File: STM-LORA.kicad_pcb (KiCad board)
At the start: 2 copper layers, 2 parts, among them U1 stm32f103c8t6-module-china, U2 RFM95HW

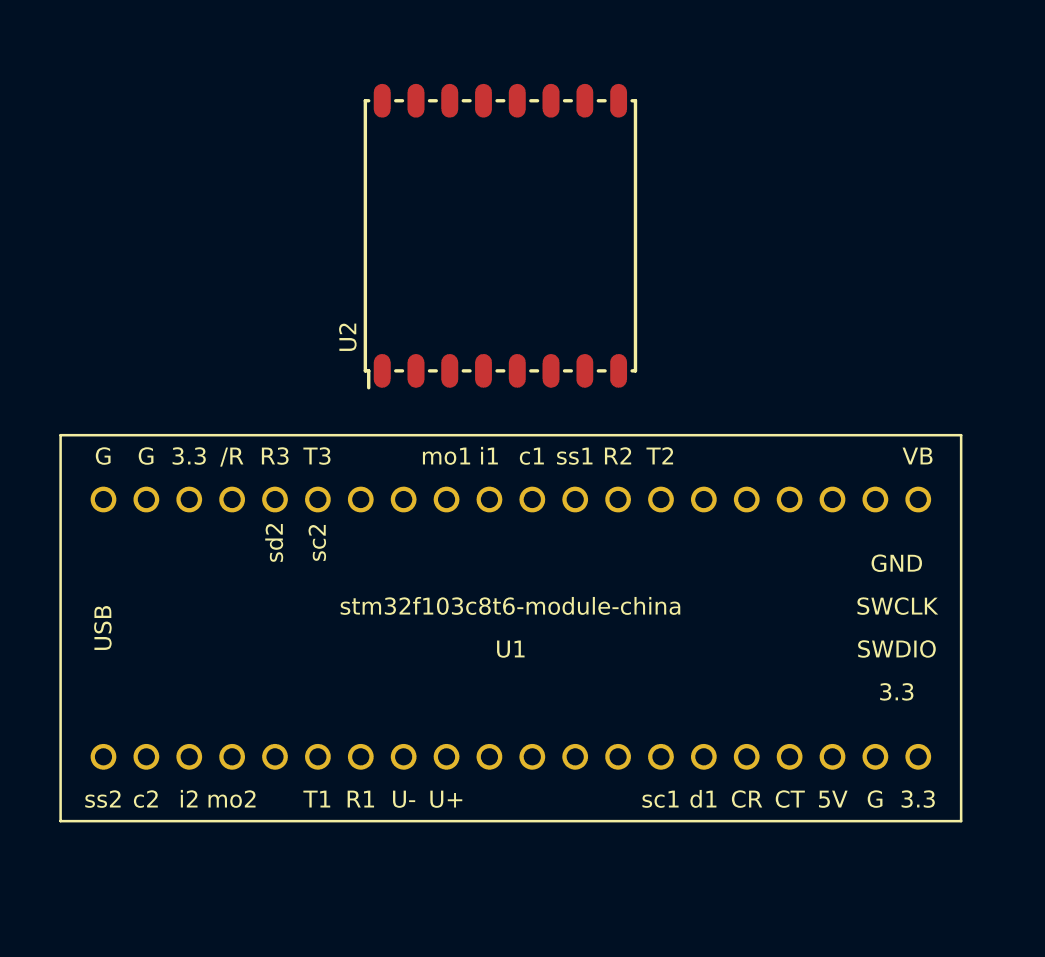
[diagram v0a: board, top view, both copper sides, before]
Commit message: Added power components
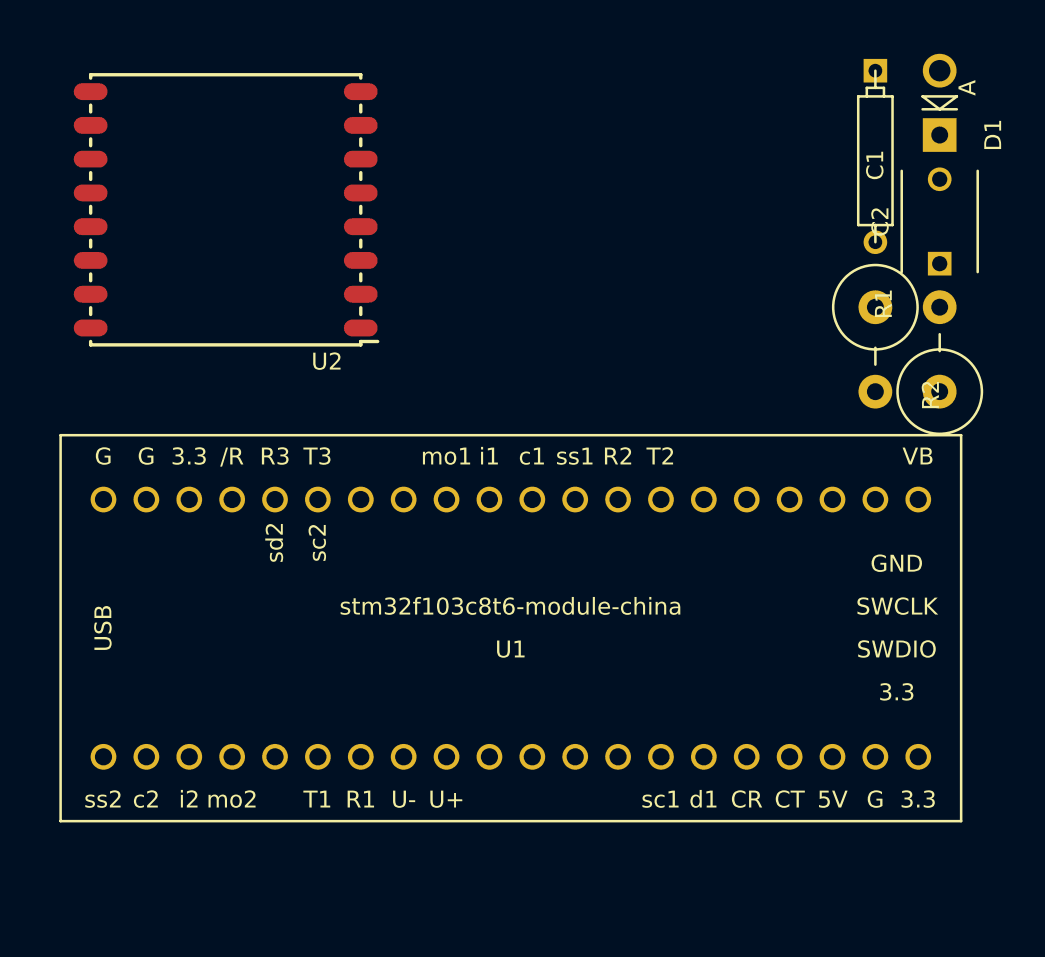
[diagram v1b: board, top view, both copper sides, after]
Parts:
- added C1: 100µ, Discret:CP4, F.Cu at (133.3, 62.2)
- added C2: 100n, Capacitors_ThroughHole:C_Disc_D6_P5, F.Cu at (137.2, 68.6)
- added D1: D_Schottky BAT85, Diodes_ThroughHole:Diode_DO-41_SOD81_Vertical_AnodeUp, F.Cu at (137.2, 61.0)
- added R1: 100k, Resistors_ThroughHole:Resistor_Vertical_RM5mm, F.Cu at (137.2, 73.7)
- added R2: 100k, Resistors_ThroughHole:Resistor_Vertical_RM5mm, F.Cu at (133.3, 73.7)
- moved U2 2.84 mm to (102.9, 72.4), turned to 180 degrees
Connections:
- net /3V3 renamed +3V3
- U1 pad 18: Net-(U1-Pad18) -> +BATT
- U1 pad 26: Net-(U1-Pad26) -> /BattTest

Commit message: update STM32 lib, add connectors
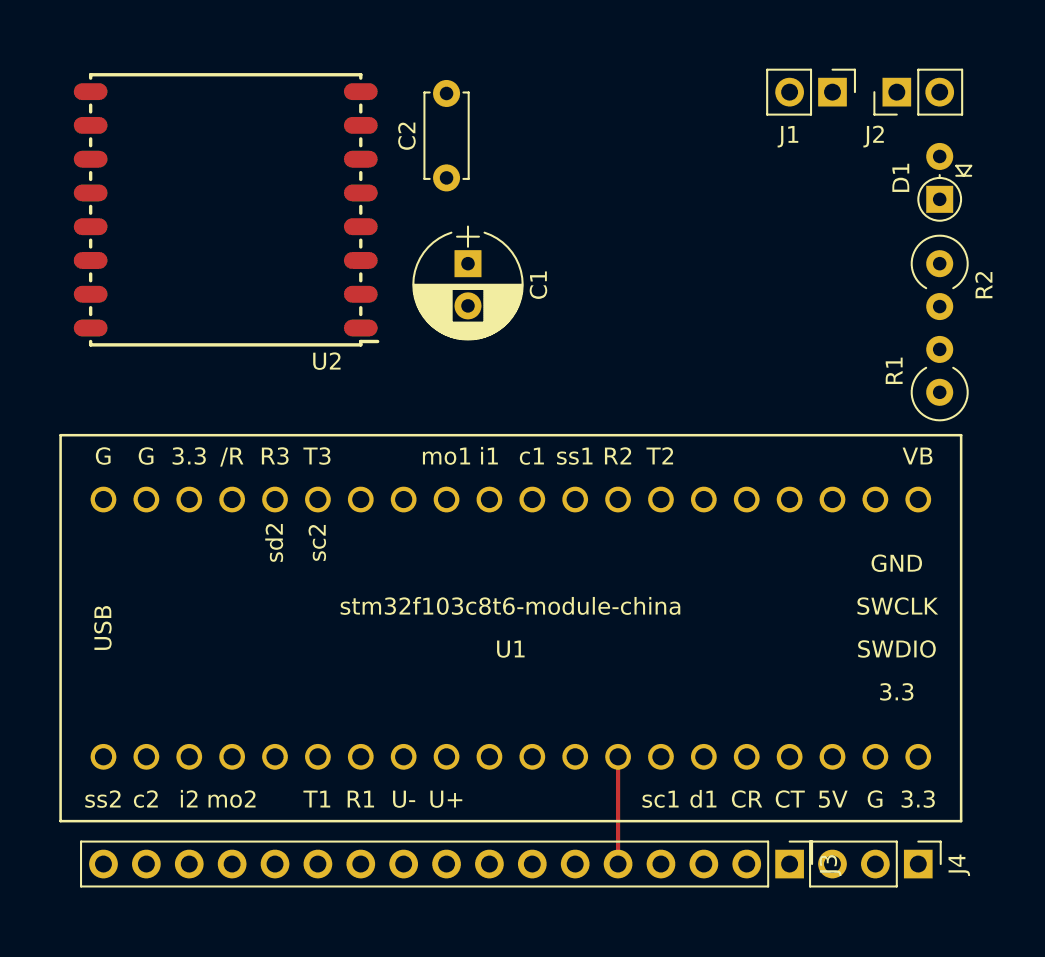
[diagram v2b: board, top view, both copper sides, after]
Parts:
- added J1: Batt, Pin_Headers:Pin_Header_Straight_1x02_Pitch2.54mm, F.Cu at (130.8, 58.4)
- added J2: Solar, Pin_Headers:Pin_Header_Straight_1x02_Pitch2.54mm, F.Cu at (134.6, 58.4)
- added J3: CONN_01X17, Socket_Strips:Socket_Strip_Straight_1x17_Pitch2.54mm, F.Cu at (128.3, 104.1)
- added J4: CONN_01X03, Pin_Headers:Pin_Header_Straight_1x03_Pitch2.54mm, F.Cu at (135.9, 104.1)
- C1: footprint Discret:CP4 -> Capacitors_THT:CP_Radial_D6.3mm_P2.50mm
- C2: footprint Capacitors_ThroughHole:C_Disc_D6_P5 -> Capacitors_THT:C_Disc_D5.0mm_W2.5mm_P5.00mm
- D1: value D_Schottky BAT85 -> BAT85; footprint Diodes_ThroughHole:Diode_DO-41_SOD81_Vertical_AnodeUp -> Diodes_THT:D_DO-35_SOD27_P2.54mm_Vertical_AnodeUp
- R1, R2: footprint Resistors_ThroughHole:Resistor_Vertical_RM5mm -> Resistors_THT:R_Axial_DIN0309_L9.0mm_D3.2mm_P2.54mm_Vertical
- moved C2 29.6 mm to (108.0, 63.5)
- moved C1 25.0 mm to (109.2, 68.6)
- moved R2 6.35 mm to (137.2, 68.6)
- moved D1 3.81 mm to (137.2, 64.8)
- moved R1 2.54 mm to (137.2, 76.2)
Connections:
- net +BATT renamed VCC
- D1 pad 2: +5V -> Net-(D1-Pad2)
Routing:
- net Net-(J3-Pad5): track 0.00 -> 6.35 mm

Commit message: start traces
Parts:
- added J5: CONN_01X03, Pin_Headers:Pin_Header_Straight_1x03_Pitch2.54mm, F.Cu at (87.6, 76.2)
- added J6: CONN_01X01, Pin_Headers:Pin_Header_Straight_1x01_Pitch2.54mm, F.Cu at (132.1, 76.2)
- added J7: CONN_01X14, Socket_Strips:Socket_Strip_Straight_1x14_Pitch2.54mm, F.Cu at (95.2, 76.2)
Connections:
- net +3V3 renamed /3V3
- net /BattTest renamed /P26
- net Net-(U1-Pad28) renamed /P28
- net Net-(U1-Pad30) renamed /P30
- net Net-(U1-Pad31) renamed /P31
- net Net-(U1-Pad32) renamed /P32
- net Net-(U1-Pad33) renamed /P33
- net Net-(U1-Pad34) renamed /P34
- U1 pad 22: Net-(U1-Pad22) -> /P22
- U1 pad 25: Net-(U1-Pad25) -> /P25
- U1 pad 27: Net-(U1-Pad27) -> /P27
- U1 pad 29: Net-(U1-Pad29) -> /P29
- U1 pad 35: Net-(U1-Pad35) -> /P35
- U1 pad 36: Net-(U1-Pad36) -> /P36
- U1 pad 37: Net-(U1-Pad37) -> /P37

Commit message: version 0.1
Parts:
- added J8: CONN_01X05, Socket_Strips:Socket_Strip_Straight_1x05_Pitch2.54mm, F.Cu at (118.1, 67.3)
- added J9: CONN_01X05, Socket_Strips:Socket_Strip_Straight_1x05_Pitch2.54mm, F.Cu at (118.1, 63.5)
- added REF**: Pin_Header_Straight_1x01_Pitch2.54mm, Pin_Headers:Pin_Header_Straight_1x01_Pitch2.54mm, F.Cu at (115.6, 69.8)
- added REF**: Pin_Header_Straight_1x01_Pitch2.54mm, Pin_Headers:Pin_Header_Straight_1x01_Pitch2.54mm, F.Cu at (133.3, 67.3)
- added REF**: Pin_Header_Straight_1x01_Pitch2.54mm, Pin_Headers:Pin_Header_Straight_1x01_Pitch2.54mm, F.Cu at (133.3, 63.5)
- added REF**: Pin_Header_Straight_1x01_Pitch2.54mm, Pin_Headers:Pin_Header_Straight_1x01_Pitch2.54mm, F.Cu at (115.6, 63.5)
- added REF**: Pin_Header_Straight_1x01_Pitch2.54mm, Pin_Headers:Pin_Header_Straight_1x01_Pitch2.54mm, F.Cu at (113.0, 63.5)
- added REF**: Pin_Header_Straight_1x01_Pitch2.54mm, Pin_Headers:Pin_Header_Straight_1x01_Pitch2.54mm, F.Cu at (113.0, 61.0)
- added REF**: Pin_Header_Straight_1x01_Pitch2.54mm, Pin_Headers:Pin_Header_Straight_1x01_Pitch2.54mm, F.Cu at (118.1, 61.0)
- added REF**: Pin_Header_Straight_1x01_Pitch2.54mm, Pin_Headers:Pin_Header_Straight_1x01_Pitch2.54mm, F.Cu at (120.7, 61.0)
- added REF**: Pin_Header_Straight_1x01_Pitch2.54mm, Pin_Headers:Pin_Header_Straight_1x01_Pitch2.54mm, F.Cu at (123.2, 61.0)
- added REF**: Pin_Header_Straight_1x01_Pitch2.54mm, Pin_Headers:Pin_Header_Straight_1x01_Pitch2.54mm, F.Cu at (125.7, 61.0)
- added REF**: Pin_Header_Straight_1x01_Pitch2.54mm, Pin_Headers:Pin_Header_Straight_1x01_Pitch2.54mm, F.Cu at (123.2, 58.4)
- added REF**: Pin_Header_Straight_1x01_Pitch2.54mm, Pin_Headers:Pin_Header_Straight_1x01_Pitch2.54mm, F.Cu at (118.1, 69.8)
- added REF**: Pin_Header_Straight_1x01_Pitch2.54mm, Pin_Headers:Pin_Header_Straight_1x01_Pitch2.54mm, F.Cu at (120.7, 58.4)
- added REF**: Pin_Header_Straight_1x01_Pitch2.54mm, Pin_Headers:Pin_Header_Straight_1x01_Pitch2.54mm, F.Cu at (118.1, 58.4)
- added REF**: Pin_Header_Straight_1x01_Pitch2.54mm, Pin_Headers:Pin_Header_Straight_1x01_Pitch2.54mm, F.Cu at (115.6, 58.4)
- added REF**: Pin_Header_Straight_1x01_Pitch2.54mm, Pin_Headers:Pin_Header_Straight_1x01_Pitch2.54mm, F.Cu at (130.8, 69.8)
- added REF**: Pin_Header_Straight_1x01_Pitch2.54mm, Pin_Headers:Pin_Header_Straight_1x01_Pitch2.54mm, F.Cu at (128.3, 72.4)
- added REF**: Pin_Header_Straight_1x01_Pitch2.54mm, Pin_Headers:Pin_Header_Straight_1x01_Pitch2.54mm, F.Cu at (130.8, 67.3)
- added REF**: Pin_Header_Straight_1x01_Pitch2.54mm, Pin_Headers:Pin_Header_Straight_1x01_Pitch2.54mm, F.Cu at (128.3, 61.0)
- added REF**: Pin_Header_Straight_1x01_Pitch2.54mm, Pin_Headers:Pin_Header_Straight_1x01_Pitch2.54mm, F.Cu at (125.7, 58.4)
- added REF**: Pin_Header_Straight_1x01_Pitch2.54mm, Pin_Headers:Pin_Header_Straight_1x01_Pitch2.54mm, F.Cu at (130.8, 63.5)
- added REF**: Pin_Header_Straight_1x01_Pitch2.54mm, Pin_Headers:Pin_Header_Straight_1x01_Pitch2.54mm, F.Cu at (125.7, 72.4)
- added REF**: Pin_Header_Straight_1x01_Pitch2.54mm, Pin_Headers:Pin_Header_Straight_1x01_Pitch2.54mm, F.Cu at (120.7, 69.8)
- added REF**: Pin_Header_Straight_1x01_Pitch2.54mm, Pin_Headers:Pin_Header_Straight_1x01_Pitch2.54mm, F.Cu at (123.2, 72.4)
- added REF**: Pin_Header_Straight_1x01_Pitch2.54mm, Pin_Headers:Pin_Header_Straight_1x01_Pitch2.54mm, F.Cu at (120.7, 72.4)
- added REF**: Pin_Header_Straight_1x01_Pitch2.54mm, Pin_Headers:Pin_Header_Straight_1x01_Pitch2.54mm, F.Cu at (118.1, 72.4)
- added REF**: Pin_Header_Straight_1x01_Pitch2.54mm, Pin_Headers:Pin_Header_Straight_1x01_Pitch2.54mm, F.Cu at (115.6, 72.4)
- added REF**: Pin_Header_Straight_1x01_Pitch2.54mm, Pin_Headers:Pin_Header_Straight_1x01_Pitch2.54mm, F.Cu at (115.6, 61.0)
- added REF**: Pin_Header_Straight_1x01_Pitch2.54mm, Pin_Headers:Pin_Header_Straight_1x01_Pitch2.54mm, F.Cu at (113.0, 58.4)
- added REF**: Pin_Header_Straight_1x01_Pitch2.54mm, Pin_Headers:Pin_Header_Straight_1x01_Pitch2.54mm, F.Cu at (113.0, 72.4)
- added REF**: Pin_Header_Straight_1x01_Pitch2.54mm, Pin_Headers:Pin_Header_Straight_1x01_Pitch2.54mm, F.Cu at (113.0, 69.8)
- added REF**: Pin_Header_Straight_1x01_Pitch2.54mm, Pin_Headers:Pin_Header_Straight_1x01_Pitch2.54mm, F.Cu at (113.0, 67.3)
- added REF**: Pin_Header_Straight_1x01_Pitch2.54mm, Pin_Headers:Pin_Header_Straight_1x01_Pitch2.54mm, F.Cu at (115.6, 67.3)
- added REF**: Pin_Header_Straight_1x01_Pitch2.54mm, Pin_Headers:Pin_Header_Straight_1x01_Pitch2.54mm, F.Cu at (123.2, 69.8)
- added REF**: Pin_Header_Straight_1x01_Pitch2.54mm, Pin_Headers:Pin_Header_Straight_1x01_Pitch2.54mm, F.Cu at (110.5, 63.5)
- added REF**: Pin_Header_Straight_1x01_Pitch2.54mm, Pin_Headers:Pin_Header_Straight_1x01_Pitch2.54mm, F.Cu at (110.5, 61.0)
- added REF**: Pin_Header_Straight_1x01_Pitch2.54mm, Pin_Headers:Pin_Header_Straight_1x01_Pitch2.54mm, F.Cu at (110.5, 58.4)
- added REF**: Pin_Header_Straight_1x01_Pitch2.54mm, Pin_Headers:Pin_Header_Straight_1x01_Pitch2.54mm, F.Cu at (125.7, 69.8)
- added REF**: Pin_Header_Straight_1x01_Pitch2.54mm, Pin_Headers:Pin_Header_Straight_1x01_Pitch2.54mm, F.Cu at (128.3, 69.8)
- added REF**: Pin_Header_Straight_1x01_Pitch2.54mm, Pin_Headers:Pin_Header_Straight_1x01_Pitch2.54mm, F.Cu at (130.8, 72.4)
- added REF**: Pin_Header_Straight_1x01_Pitch2.54mm, Pin_Headers:Pin_Header_Straight_1x01_Pitch2.54mm, F.Cu at (133.3, 72.4)
- added REF**: Pin_Header_Straight_1x01_Pitch2.54mm, Pin_Headers:Pin_Header_Straight_1x01_Pitch2.54mm, F.Cu at (133.3, 69.8)
- moved R1 7.62 mm to (137.2, 68.6), turned to 270 degrees
- moved C2 5.12 mm to (107.3, 58.4), turned to 270 degrees
- moved R2 5.08 mm to (137.2, 73.7)
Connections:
- net Net-(D1-Pad2) renamed /Solar
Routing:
- net GND: track 0.00 -> 280.9 mm, vias 0 -> 6
- net /3V3: track 0.00 -> 127.4 mm, vias 0 -> 3
- net Net-(J3-Pad5): track 6.35 -> 66.6 mm
- net VCC: track 0.00 -> 56.1 mm
- net /P28: track 0.00 -> 41.7 mm, vias 0 -> 2
- net /P34: track 0.00 -> 26.0 mm, vias 0 -> 2
- net /P26: track 0.00 -> 25.8 mm
- net /P33: track 0.00 -> 21.8 mm, vias 0 -> 2
- net /P30: track 0.00 -> 21.7 mm, vias 0 -> 2
- net /P32: track 0.00 -> 16.9 mm, vias 0 -> 2
- net /P31: track 0.00 -> 16.4 mm, vias 0 -> 2
- net /P22: track 0.00 -> 8.45 mm
- net Net-(J6-Pad1): track 0.00 -> 7.93 mm
- net Net-(J3-Pad9): track 0.00 -> 6.35 mm
- net Net-(J3-Pad8): track 0.00 -> 6.35 mm
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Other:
- net class Power added: clearance 0.2, trace_width 0.5, via_dia 0.6, via_drill 0.4
- board text added: "100k"
- board text added: "100n"
- board text added: "100µ"
- board text added: "3V3"
- board text added: "BAT85"
- board text added: "Bat"
- board text added: "GND"
- board text added: "STM32 - RFM95 Proto Board v0.1"
- board text added: "Slr"
- board text added: "http://v7f.eu (C) 2017"

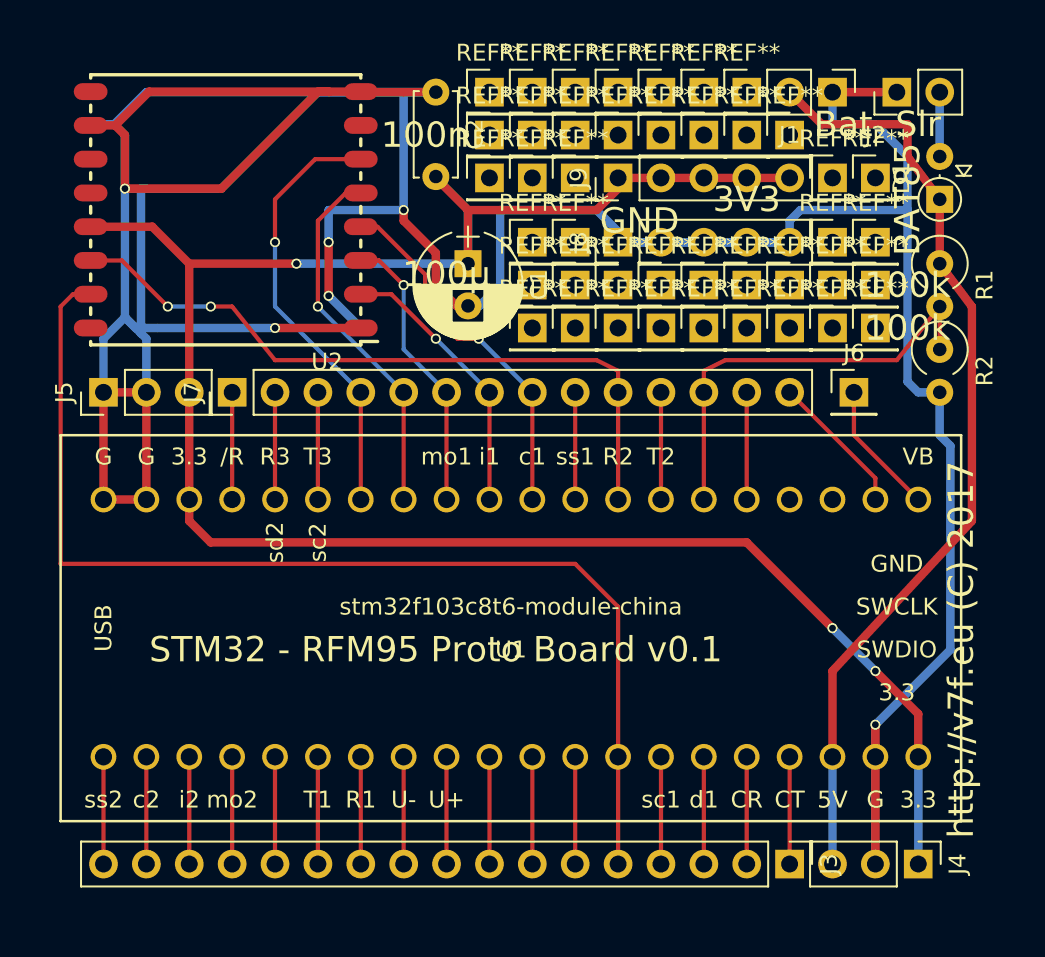
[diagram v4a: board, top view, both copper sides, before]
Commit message: Update edges, silk screen
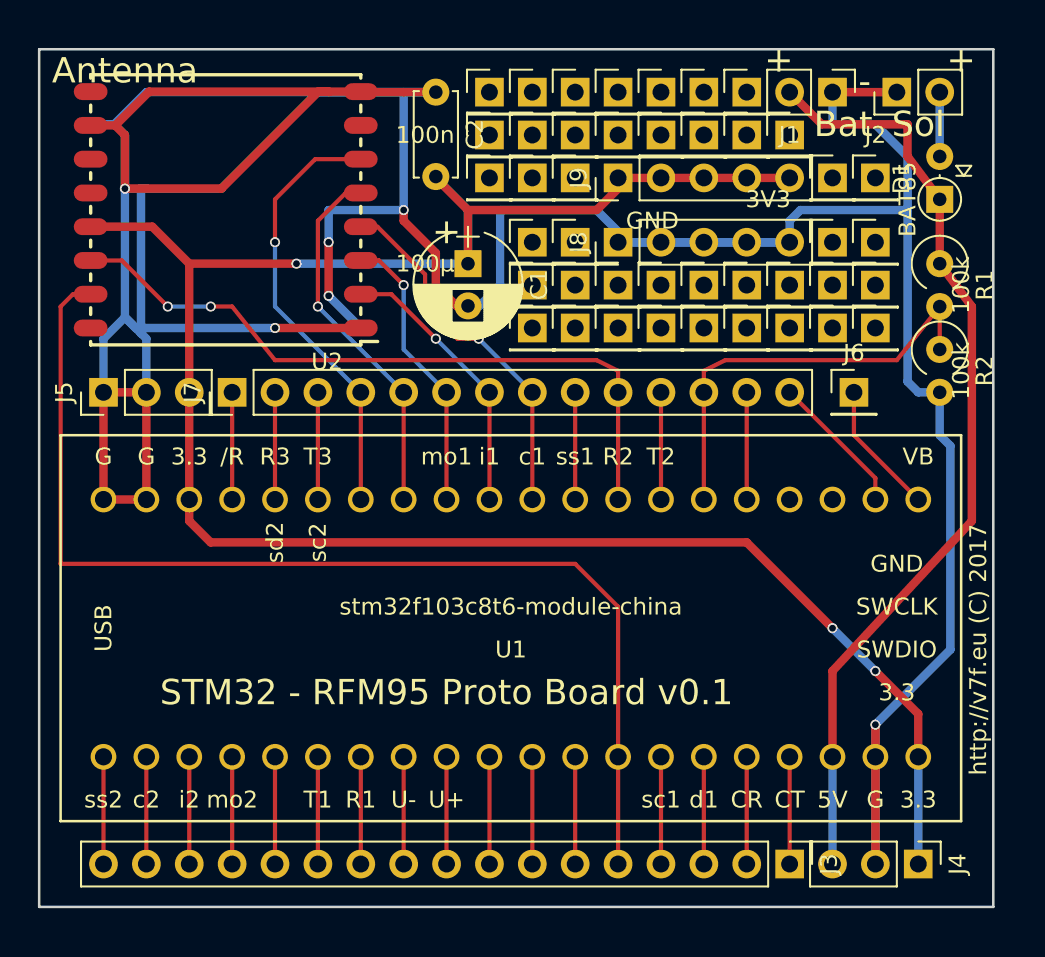
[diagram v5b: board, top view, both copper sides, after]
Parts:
- renumbered REF** to ?
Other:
- board outline added: 56.5 x 50.8 mm
- board text added: "+"
- board text added: "-"
- board text added: "Antenna"
- board text added: "Sol"
- board text removed: "Slr"
